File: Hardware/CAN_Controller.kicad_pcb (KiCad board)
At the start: 2 copper layers, 30 x 24.2 mm, 21 parts, among them J1 Conn_01x03, J2 Conn_01x08, J3 Conn_01x02, U1 ATtiny814-SS, U2 MCP2515-xSO, U3 MCP2551-I-SN, U4 MCP16331CH, Y1 8 MHz

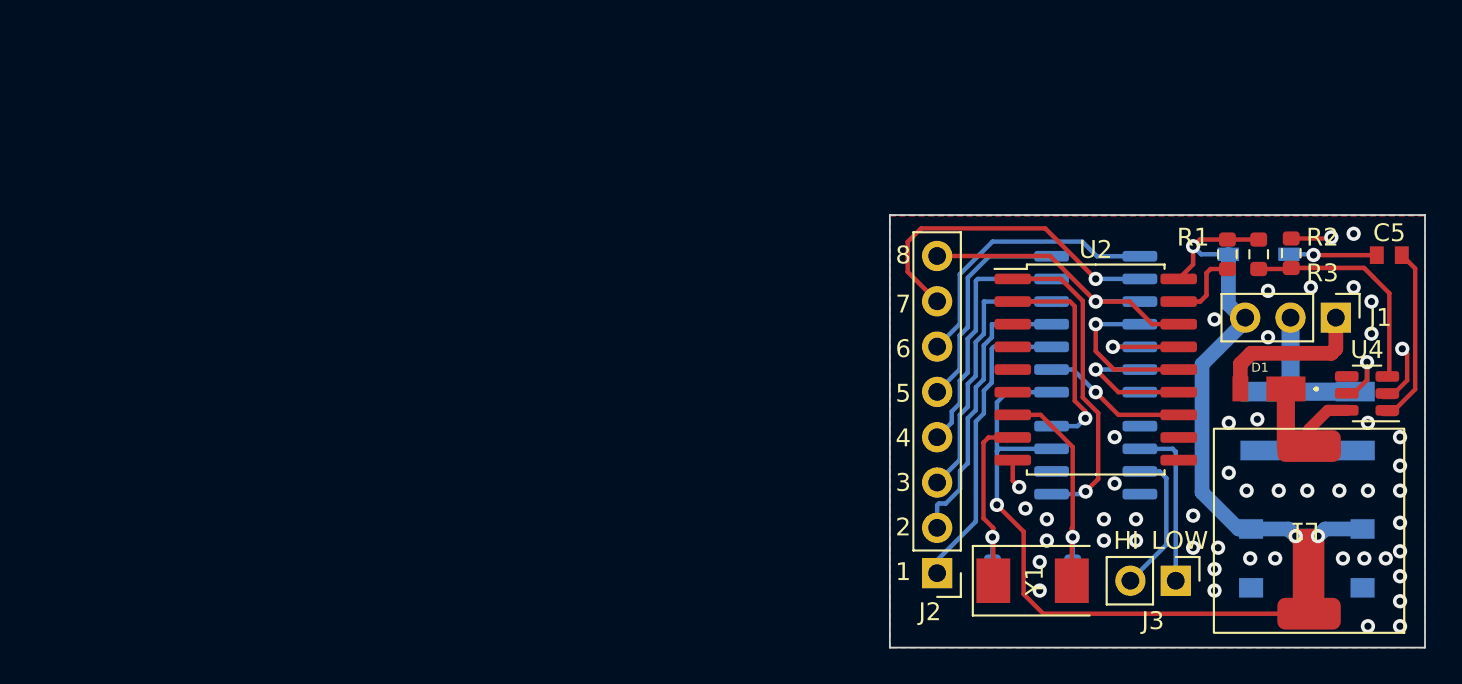
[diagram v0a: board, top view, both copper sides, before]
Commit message: rearrainged components to reduce board size and added project footprints
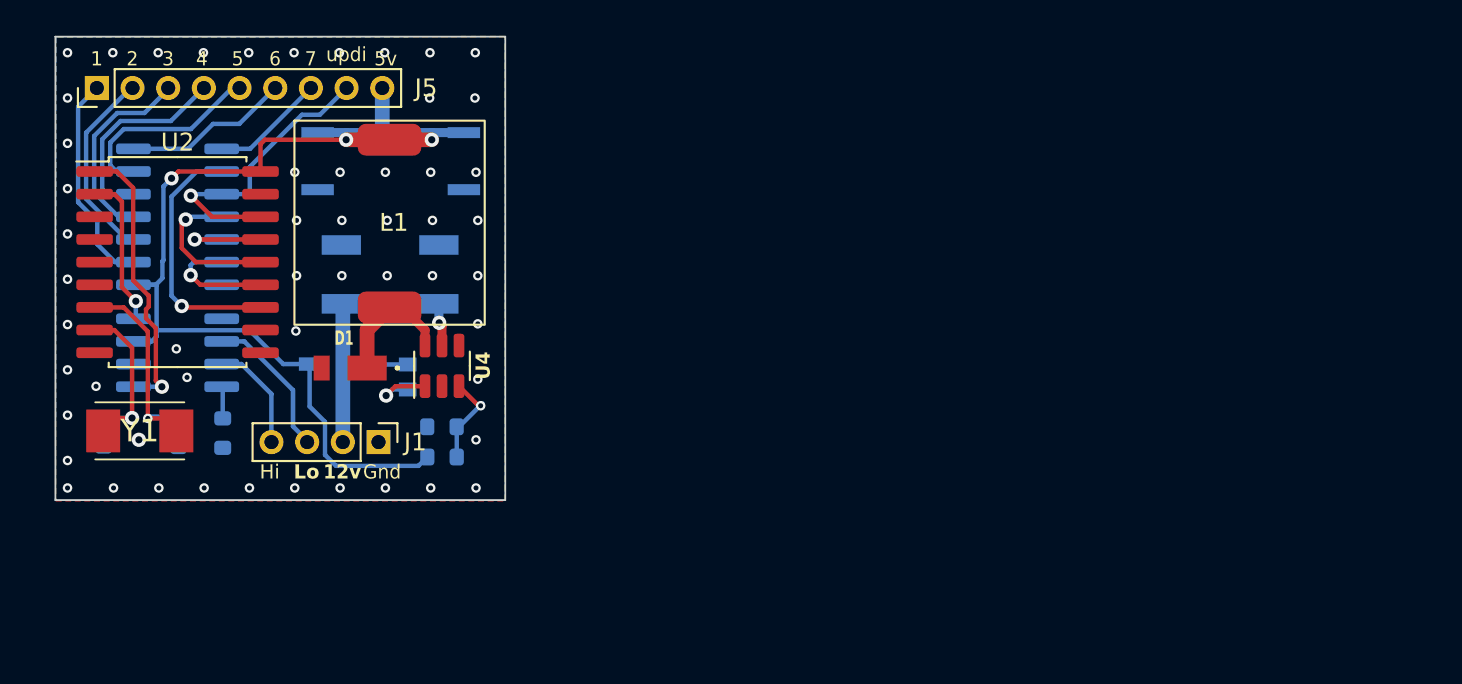
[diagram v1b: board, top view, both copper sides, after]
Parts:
- removed J2: Conn_01x08, Connector_PinHeader_2.54mm:PinHeader_1x08_P2.54mm_Vertical
- removed J3: Conn_01x02, Connector_PinHeader_2.54mm:PinHeader_1x02_P2.54mm_Vertical
- added J5: Conn_01x09, Connector_PinHeader_2.00mm:PinHeader_1x09_P2.00mm_Vertical, F.Cu at (122.8, 75.9)
- C3, C4: value C3225X7R1H106M250AC -> 10uF
- C5: value 0603YC104KAT2A -> 100 nF; moved to B.Cu
- C6, C7: footprint C3216_Commercial:C3216_Commercial -> CAPC3216X180N:CAPC3216X180N
- D2: footprint 1N4148_SOD_SMD:SOD3716X145N -> 1N4148WQ-7-F:SOD3716X145N
- J1: value Conn_01x03 -> Conn_01x04; footprint Connector_PinHeader_2.54mm:PinHeader_1x03_P2.54mm_Vertical -> Connector_PinHeader_2.00mm:PinHeader_1x04_P2.00mm_Vertical
- L1: value MSS1048-223 -> 22 µH
- R1: value 10 k -> 10; moved to B.Cu
- R2, R3: moved to B.Cu
- Y1: footprint Crystal:Crystal_SMD_0603-2Pin_6.0x3.5mm -> ECS-80-8-30Q-VS-TR:ECS80830QVSTR
- moved C6 62.7 mm to (135.2, 80.0)
- moved C3 57.4 mm to (136.5, 86.3), turned to -90 degrees
- moved R1 57.2 mm to (129.8, 95.2)
- moved C5 55.5 mm to (140.2, 92.1), turned to 90 degrees
- moved L1 54.4 mm to (139.2, 83.4), turned to 0 degrees
- moved J1 54.1 mm to (138.6, 95.7)
- moved U4 51.9 mm to (142.1, 91.5), turned to 90 degrees
- moved D2 51.9 mm to (136.4, 91.4)
- moved U1 51.8 mm to (127.3, 83.1)
- moved U2 51.8 mm to (127.3, 85.6)
- moved U3 51.8 mm to (127.3, 90.7)
- moved D1 51.5 mm to (137.0, 91.6)
- moved C2 50.8 mm to (127.4, 95.2)
- moved Y1 50.7 mm to (125.2, 95.1), turned to 180 degrees
- moved C1 50.5 mm to (123.2, 95.2)
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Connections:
- C1 pad 1: Net-(C1-Pad1) -> Net-(U2-OSC1)
- C2 pad 1: Net-(C2-Pad1) -> Net-(U2-OSC2)
- J1 pad 3: Vos -> CAN L
- R1 pad 1: Net-(R1-Pad1) -> GND
- R1 pad 2: Vos -> Net-(U3-Rs)
- U1 pad 2: Net-(U1-Pad2) -> Net-(J5-Pin_1)
- U1 pad 9: Net-(J2-Pad7) -> Net-(U1-PB0)
- U2 pad 12: Net-(U1-Pad2) -> Net-(U1-PB0)
- U2 pad 17: Net-(R1-Pad1) -> unconnected-(U2-~{RESET}-Pad17)
- U2 pad 7: Net-(C2-Pad1) -> Net-(U2-OSC2)
- U2 pad 8: Net-(C1-Pad1) -> Net-(U2-OSC1)
- U3 pad 8: GND -> Net-(U3-Rs)
- Y1 pad 1: Net-(C1-Pad1) -> Net-(U2-OSC2)
- Y1 pad 2: Net-(C2-Pad1) -> Net-(U2-OSC1)
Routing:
- net Net-(J2-Pad7): track 18.5 -> 0.00 mm, vias 1 -> 0
- net GND: track 16.8 -> 0.00 mm, vias 50 -> 54
- net Vos: track 82.6 -> 68.2 mm, vias 4 -> 3
- net Net-(U1-PB0): track 0.00 -> 14.2 mm, vias 0 -> 1
- net Net-(C2-Pad1): track 12.6 -> 0.00 mm, vias 1 -> 0
- net Net-(J5-Pin_1): track 0.00 -> 12.1 mm
- net Net-(U2-OSC2): track 0.00 -> 12.0 mm, vias 0 -> 1
- net Net-(C1-Pad1): track 10.6 -> 0.00 mm, vias 1 -> 0
- net Net-(U2-OSC1): track 0.00 -> 9.97 mm, vias 0 -> 1
- net Net-(J5-Pin_7): track 15.8 -> 6.41 mm
- net Net-(U1-Pad2): track 8.18 -> 0.00 mm, vias 1 -> 0
- net Net-(U4-VFB): track 12.7 -> 5.36 mm, vias 0 -> 1
- net Net-(U4-BOOST): track 10.6 -> 3.75 mm, vias 0 -> 1
- net Net-(J5-Pin_2): track 17.2 -> 10.9 mm
- net Net-(J5-Pin_3): track 16.3 -> 11.2 mm
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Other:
- board size 30 x 24.2 mm -> 25.2 x 26 mm
- board text added: "12v"
- board text added: "Gnd"
- board text added: "Hi"
- board text added: "Lo"
- board text added: "updi"
- board text removed: "8"
- board text removed: "GND"
- board text removed: "HI"
- board text removed: "LOW"
- board text removed: "Vin"

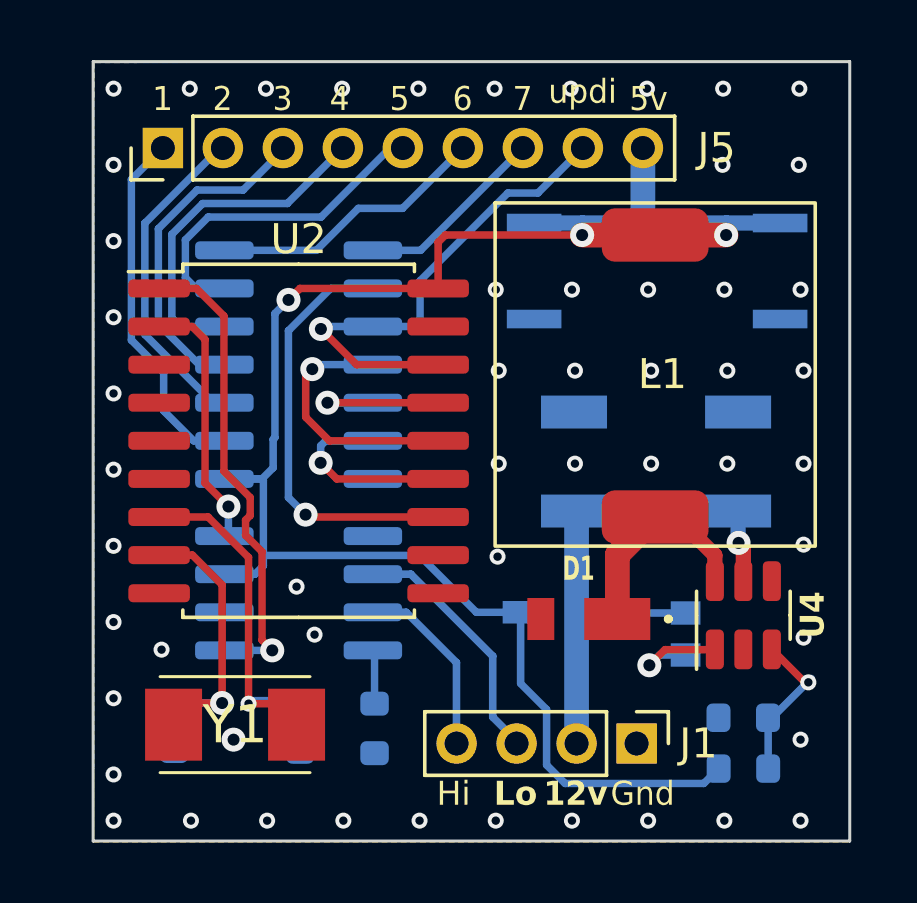
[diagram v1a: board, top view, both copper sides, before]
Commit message: Reduced PCB footprint
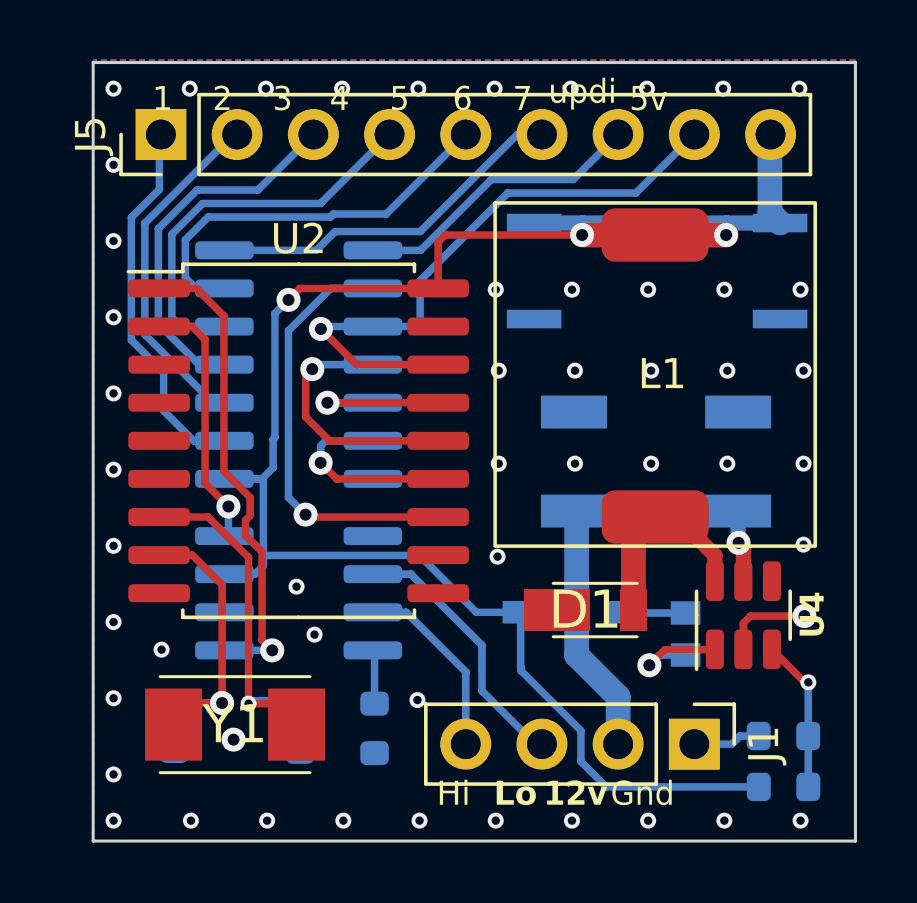
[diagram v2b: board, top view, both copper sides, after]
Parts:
- D1: value D_Schottky -> DFLS120LQ-7; footprint Schottky_Diode:DFLS120L7 -> DFLS120LQ-7:DFLS120LQ7
- J1: footprint Connector_PinHeader_2.00mm:PinHeader_1x04_P2.00mm_Vertical -> Connector_PinHeader_2.54mm:PinHeader_1x04_P2.54mm_Vertical
- J5: footprint Connector_PinHeader_2.00mm:PinHeader_1x09_P2.00mm_Vertical -> Connector_PinHeader_2.54mm:PinHeader_1x09_P2.54mm_Vertical
- R1: value 10 -> 10 KOhms
- moved J1 1.93 mm to (140.5, 95.8)
- moved R2 1.47 mm to (143.5, 95.5)
- moved R3 1.47 mm to (143.5, 97.2)
- moved J5 0.45 mm to (122.7, 75.4)
- moved D1 0.37 mm to (137.2, 91.3), turned to 0 degrees
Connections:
- D1 pad 1: Net-(D1-K) -> GND
- D1 pad 2: GND -> Net-(D1-K)
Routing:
- net GND: track 0.00 -> 5.27 mm, vias 54 -> 52
- net Net-(J5-Pin_8): track 16.5 -> 20.4 mm
- net Net-(J5-Pin_7): track 6.41 -> 9.77 mm
- net Net-(J5-Pin_6): track 9.36 -> 12.2 mm
- net Net-(J5-Pin_5): track 11.2 -> 13.5 mm
- net Net-(J5-Pin_4): track 11.6 -> 13.7 mm
- net Net-(J5-Pin_3): track 11.2 -> 12.4 mm
- net Vos: track 68.2 -> 69.3 mm
- net Net-(J5-Pin_2): track 10.9 -> 11.6 mm
- net Vdd: track 15.7 -> 16.3 mm
- net Net-(D1-K): track 7.30 -> 6.78 mm
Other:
- board size 25.2 x 26 mm -> 25.4 x 26 mm
